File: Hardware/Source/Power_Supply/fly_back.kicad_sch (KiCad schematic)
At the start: 45 parts, among them J1 HB9500M-9.5-3P, U1 TOP270VG, U3 PC817X2NIPW, U4 TL431CLPM

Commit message: update
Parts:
- R11: value 4.99K 1206 1% -> 4.99K/1206/1%
- U2: footprint (none) -> charge_battery_footprint_lib:Transformer_ER35
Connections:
- net at C11.1, U3.4 (C): now also D3.2; no longer D3.
- net at U2.6 (OUT2A): now also D3.1; no longer D3.
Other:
- moved on the sheet: D3
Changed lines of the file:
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@@
 	(wire
 		(pts
-			(xy 257.81 102.87) (xy 264.16 102.87)
+			(xy 254 102.87) (xy 264.16 102.87)
 		)
 		(stroke
@@
 	(wire
 		(pts
-			(xy 238.76 102.87) (xy 247.65 102.87)
+			(xy 238.76 102.87) (xy 243.84 102.87)
 		)
 		(stroke
@@
 			)
 		)
-		(property "Value" "4.99K 1206 1%"
+		(property "Value" "4.99K/1206/1%"
 			(at 307.34 120.6499 90)
 			(effects
@@
 			)
 		)
-		(property "Footprint" ""
+		(property "Footprint" "charge_battery_footprint_lib:Transformer_ER35"
 			(at 228.6 87.63 0)
 			(effects
@@
 	(symbol
 		(lib_id "charge_battery_sym_lib:1N914")
-		(at 247.65 102.87 0)
+		(at 243.84 102.87 0)
 		(unit 1)
 		(exclude_from_sim no)
@@
 		(dnp no)
 		(property "Reference" "D3"
-			(at 252.984 99.568 0)
+			(at 249.174 99.568 0)
 			(effects
 				(font
@@
 		)
 		(property "Value" "1N914"
-			(at 252.984 106.172 0)
+			(at 249.174 106.172 0)
 			(effects
 				(font
@@
 		)
 		(property "Footprint" "charge_battery_footprint_lib:DO-204AH"
-			(at 252.984 109.474 0)
+			(at 249.174 109.474 0)
 			(effects
 				(font
@@
 		)
 		(property "Datasheet" "https://www.mouser.vn/datasheet/2/268/1N914-3499939.pdf"
-			(at 253.492 109.728 0)
+			(at 249.682 109.728 0)
 			(effects
 				(font
@@
 		)
 		(property "Description" "Small Signal Switching Diodes 100 V Signal or Computer Diode"
-			(at 257.81 109.728 0)
+			(at 254 109.728 0)
 			(effects
 				(font
@@
 		)
 		(property "Supply Name" "Mouser"
-			(at 252.73 109.982 0)
+			(at 248.92 109.982 0)
 			(effects
 				(font
@@
 		)
 		(property "Supply Number" "1N914"
-			(at 255.27 109.982 0)
+			(at 251.46 109.982 0)
 			(effects
 				(font
@@
 			)
 		)
-		(pin ""
+		(pin "1"
 		)
-		(pin ""
+		(pin "2"
 		)
 		(instances

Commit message: update
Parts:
- removed U2: ~, charge_battery_footprint_lib:Transformer_ER35, symbol charge_battery_sym_lib:Transformer_flyback
- added L4: EER35_Transformer_Horizontal, charge_battery_footprint_lib:Transformer_ER35_Horizontal, symbol charge_battery_sym_lib:EER35_Transformer_Horizontal
- R1, R2: value 10.2M/1% -> 10.2M/1%/1.25W
- R10: value 6.8R/0805/5% -> 6.8R/5%/1_8W
- R11: value 4.99K/1206/1% -> 4.99K/1%/1_4W
- R13: value 47.5K/1% -> 47.5K/1%/1_8W
- R14: value 12.4K/1% -> 12.4K/1%/1_8W
- R4, R5: value 2M/1% -> 2M/1%/1_10W
- R8: value 5.6R/5% -> 5.6R/5%/1_4W
- R9: value 22R/1206/1% -> 22R/1%/1_4W
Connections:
- net GND2: now also R14.1, U4.3 (A), L4.11 (SC)
- net at C5.1, C6.2, C7.1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: now also L4.1 (AA)
- net at CR2.2, R9.1: now also L4.9 (SA)
- net at CR1.2 (A), U1.6 (D): now also L4.8 (AB)
- net at C11.2: now also L4.16 (SB)
- net at D3.1: now also L4.12 (SC)
- no-connect marks 1 -> 0
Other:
- moved on the sheet: C11, C12, C13, C14, C15, C16, C5, C7, CR2, D1, L2, R4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

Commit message: update pcb flyback
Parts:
- R9: value 22R/1%/1_4W -> 22R/1%/2W; footprint charge_battery_footprint_lib:Res_1206 -> charge_battery_footprint_lib:Res_Hole_2W
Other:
- moved on the sheet: R9
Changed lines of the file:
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@@
 	(wire
 		(pts
-			(xy 254 80.01) (xy 255.27 80.01)
+			(xy 252.73 80.01) (xy 255.27 80.01)
 		)
 		(stroke
@@
 	(wire
 		(pts
-			(xy 242.57 80.01) (xy 246.38 80.01)
+			(xy 242.57 80.01) (xy 245.11 80.01)
 		)
 		(stroke
@@
 	(symbol
 		(lib_id "charge_battery_sym_lib:Res_22R_1206_1%")
-		(at 250.19 76.2 0)
+		(at 248.92 76.2 0)
 		(unit 1)
 		(exclude_from_sim no)
@@
 		(dnp no)
 		(property "Reference" "R9"
-			(at 249.936 75.946 0)
-			(effects
-				(font
-					(size 1.27 1.27)
-				)
-			)
-		)
-		(property "Value" "22R/1%/1_4W"
-			(at 248.412 77.978 0)
-			(effects
-				(font
-					(size 1.27 1.27)
-				)
-			)
-		)
-		(property "Footprint" "charge_battery_footprint_lib:Res_1206"
-			(at 250.19 76.2 0)
+			(at 248.666 75.946 0)
+			(effects
+				(font
+					(size 1.27 1.27)
+				)
+			)
+		)
+		(property "Value" "22R/1%/2W"
+			(at 247.142 77.978 0)
+			(effects
+				(font
+					(size 1.27 1.27)
+				)
+			)
+		)
+		(property "Footprint" "charge_battery_footprint_lib:Res_Hole_2W"
+			(at 248.92 76.2 0)
 			(effects
 				(font
@@
 		)
 		(property "Datasheet" ""
-			(at 250.19 76.2 0)
+			(at 248.92 76.2 0)
 			(effects
 				(font
@@
 		)
 		(property "Description" "Resistor"
-			(at 250.19 76.2 0)
+			(at 248.92 76.2 0)
 			(effects
 				(font
@@
 		)
 		(property "Supply Name" "thegioiic"
-			(at 250.19 76.2 0)
+			(at 248.92 76.2 0)
 			(effects
 				(font
@@
 		)
 		(property "Supply Part Number" "Điện Trở 22 Ohm 1206 1%"
-			(at 250.19 76.2 0)
+			(at 248.92 76.2 0)
 			(effects
 				(font
@@
 		)
 		(property "Supply URL" "https://www.thegioiic.com/dien-tro-22-ohm-1206-1-"
-			(at 250.19 76.2 0)
-			(effects
-				(font
+			(at 248.92 76.2 0)
+			(effects
+				(font

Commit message: tuan uupdate lib
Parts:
- removed L4: EER35_Transformer_Horizontal, charge_battery_footprint_lib:Transformer_ER35_Horizontal, symbol charge_battery_sym_lib:EER35_Transformer_Horizontal
- added T1: Transformer_flyback, charge_battery_footprint_lib:Transformer_ER35_Horizontal, symbol charge_battery_sym_lib:Transformer_flyback
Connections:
- net GND1: now also C11.2, R3.1, T1.5 (OUT2B)
- net GND2: now also T1.11 (OUT1B)
- net at C5.1, C6.2, C7.1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: now also R7.1, T1.1 (IN+)
- net at C6.1, D2.1 (K), R7.2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: now also R6.2
- net at CR2.2, R9.1: now also T1.9 (OUT1A)
- net at CR1.2 (A), U1.6 (D): now also T1.3 (IN-)
- net at D3.1: now also T1.14 (OUT2A)
- net at U1.2 (X): now also R2.1, R3.2; no longer R3.1
- no-connect marks 0 -> 1
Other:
- moved on the sheet: C11, C12, C13, C14, C16, CR2, L2, R6, R7

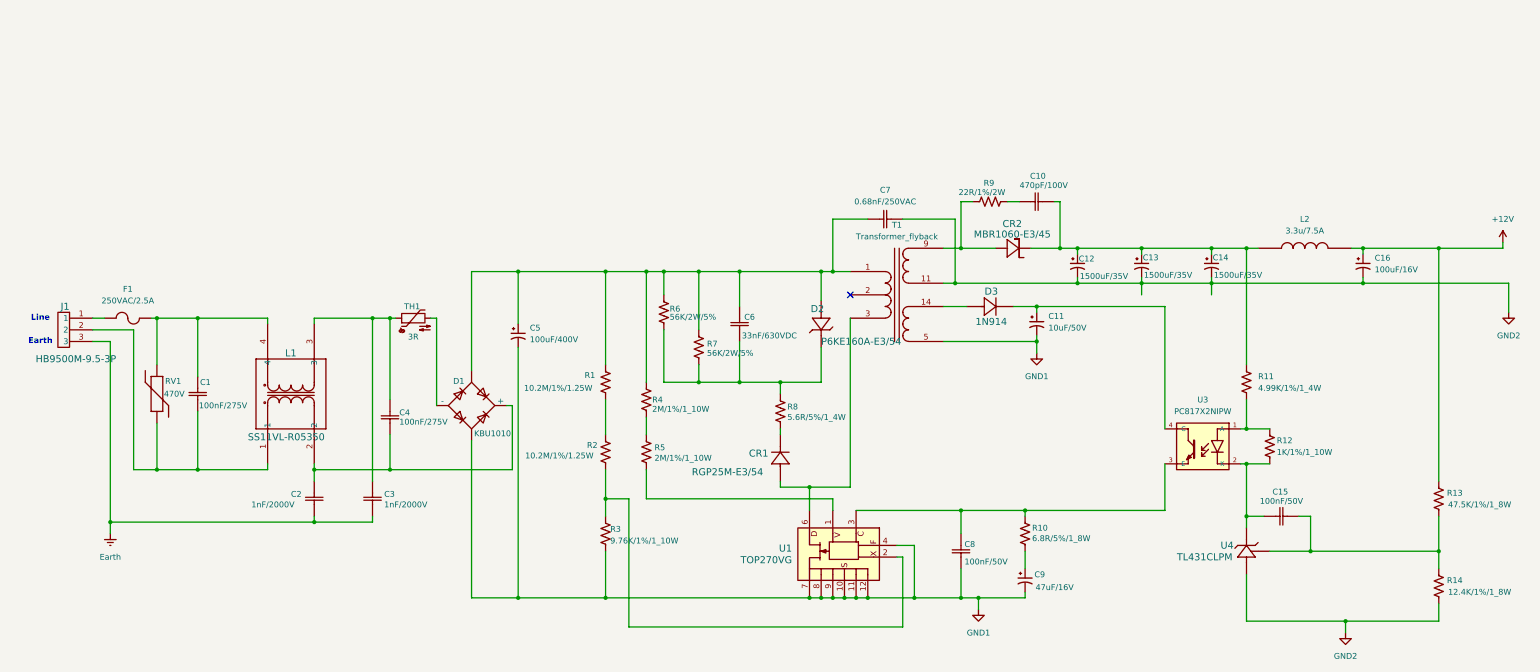
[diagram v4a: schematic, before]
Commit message: flyback 7V
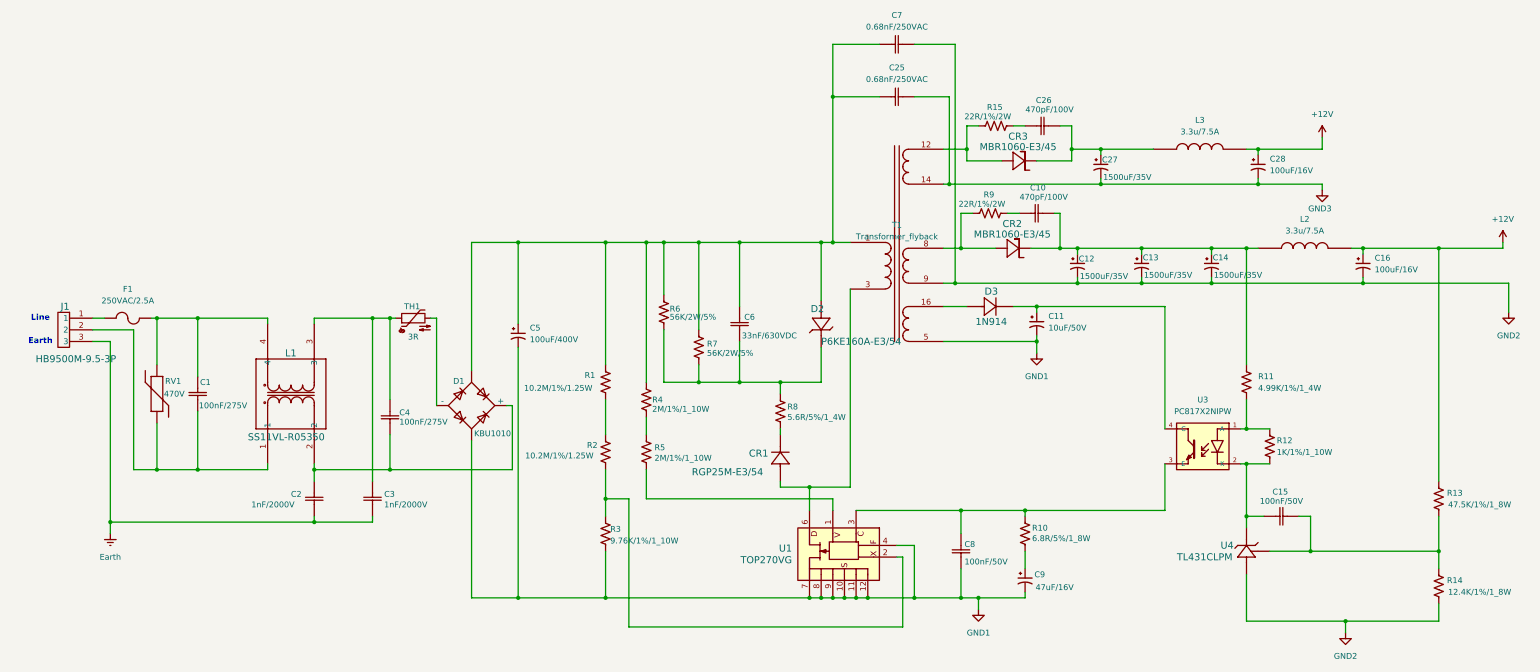
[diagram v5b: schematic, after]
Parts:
- added C25: 0.68nF/250VAC, charge_battery_footprint_lib:Ceramic_Cap_Hole_5mm, symbol charge_battery_sym_lib:EMI_Cap_Hole_0.68nF_250VAC
- added C26: 470pF/100V, charge_battery_footprint_lib:Ceramic_Cap_Hole_5mm, symbol charge_battery_sym_lib:Cap_Hole_470pF_100V
- added C27: 1500uF/35V, Capacitor_THT:CP_Radial_D13.0mm_P5.00mm, symbol charge_battery_sym_lib:Cap_Hole_1500uF_35V
- added C28: 100uF/16V, Capacitor_SMD:CP_Elec_6.3x5.4, symbol charge_battery_sym_lib:Cap_Polarize_100uF_16V
- added CR3: MBR1060-E3/45, charge_battery_footprint_lib:TO-220-2_MCH, symbol charge_battery_sym_lib:MBR1060-E3_45
- added L3: 3.3u/7.5A, charge_battery_footprint_lib:Inductor_3.3u_7447471033, symbol charge_battery_sym_lib:Inductor_3.3u_7.5A
- added R15: 22R/1%/2W, charge_battery_footprint_lib:Res_Hole_2W, symbol charge_battery_sym_lib:Res_22R_1206_1%
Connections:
- net +12V: now also C28.1, L3.2
- net GND2: now also T1.9 (OUT1B); no longer T1.11 (OUT1B)
- net at C5.1, C6.2, C7.1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: now also C25.1
- net at CR2.2, R9.1: now also T1.8 (OUT1A); no longer T1.9 (OUT1A)
- net at D3.1: now also T1.16 (OUT2A); no longer T1.14 (OUT2A)
- new net: C26.2, C27.1, CR3.1, L3.1
- new net: CR3.2, R15.1, T1.12 (OUT1A)
- new net: C26.1, R15.2
- new net GND3: C25.2, C27.2, C28.2, T1.14 (OUT1B)
- no-connect marks 1 -> 0
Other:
- moved on the sheet: C10, C7, R9

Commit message: update
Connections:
- net +12V: no longer C28.1, L3.2
- new net +7V: C28.1, L3.2
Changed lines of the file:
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@@
 			)
 		)
-		(property "Value" "+12V"
+		(property "Value" "+7V"
 			(at 321.31 60.96 0)
 			(effects

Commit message: update sche
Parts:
- removed L1: SS11VL-R05350, charge_battery_footprint_lib:IND_SS11VL-R05350_KEM, symbol charge_battery_sym_lib:SS11VL-R05350
- added FL1: SC-02-E60JKH, charge_battery_footprint_lib:SC02E60JKH, symbol charge_battery_sym_lib:SC-02-E60JKH
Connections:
- net at C2.1, C4.1, D1.1 (+): now also FL1.2
- net at C1.1, J1.2, RV1.1: now also FL1.1
- net at C1.2, F1.2, RV1.2: now also FL1.4
- net at C3.1, C4.2, TH1.1: now also FL1.3
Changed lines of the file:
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@@
-	)
-	(symbol
-		(lib_id "charge_battery_sym_lib:SS11VL-R05350")
-		(at 91.44 137.16 90)
-		(unit 1)
-		(exclude_from_sim no)
-		(in_bom yes)
-		(on_board yes)
-		(dnp no)
-		(property "Reference" "L1"
-			(at 95.25 113.03 90)
-			(effects
-				(font
-					(size 1.524 1.524)
-				)
-				(justify right)
-			)
-		)
-		(property "Value" "SS11VL-R05350"
-			(at 87.122 131.318 90)
-			(effects
-				(font
-					(size 1.524 1.524)
-				)
-				(justify right)
-			)
-		)
-		(property "Footprint" "charge_battery_footprint_lib:IND_SS11VL-R05350_KEM"
-			(at 111.506 137.922 0)
-			(effects
-				(font
-					(size 1.27 1.27)
-					(italic yes)
-				)
-				(hide yes)
-			)
-		)
-		(property "Datasheet" "https://www.mouser.vn/datasheet/2/447/KEM_LF0022_SS11VL-3316893.pdf"
-			(at 111.252 132.588 0)
-			(effects
-				(font
-					(size 1.27 1.27)
-					(italic yes)
-				)
-				(hide yes)
-			)
-		)
-		(property "Description" "Common Mode Chokes / Filters 250VAC 1.1A 5mH DCR=400mOhms"
-			(at 111.506 135.382 0)
-			(effects
-				(font
-					(size 1.27 1.27)
-				)
-				(hide yes)
-			)
-		)
-		(property "Supply name" "Mouser"
-			(at 111.506 137.668 0)
-			(effects
-				(font
-					(size 1.27 1.27)
-				)
-				(hide yes)
-			)
-		)
-		(property "Supply part number" "80-SS11VL-11050"
-			(at 111.506 137.16 0)
-			(effects
-				(font
-					(size 1.27 1.27)
-				)
-				(hide yes)
-			)
-		)
-		(property "Supply URL" "https://www.mouser.vn/ProductDetail/KEMET/SS11VL-11050?qs=EU6FO9ffTwcryP%252B%2F%252BYgxUg%3D%3D"
-			(at 111.506 149.352 0)
-			(effects
-				(font
-					(size 1.27 1.27)
-				)
-				(hide yes)
-			)
-		)
-		(pin "1"
-		)
-		(pin "2"
-		)
-		(pin "3"
-		)
-		(pin "4"
-		)
-		(instances
-			(project "Power_Supply"
-				(path "/5c8a7907-026b-4416-b231-5ef9f93b99e1/5a1d07e8-1900-453e-ab71-30ad5bc9dcd9"
-					(reference "L1")
-					(unit 1)
-				)
-			)
-		)
 	)
 	(symbol
@@
 					(unit 1)
 				)
+			)
+		)
+	)
+	(symbol
+		(lib_id "charge_battery_sym_lib:SC-02-E60JKH")
+		(at 85.09 121.92 90)
+		(unit 1)
+		(exclude_from_sim no)
+		(in_bom yes)
+		(on_board yes)
+		(dnp no)
+		(fields_autoplaced yes)
+		(property "Reference" "FL1"
+			(at 105.41 121.9199 90)
+			(effects
+				(font
+					(size 1.27 1.27)
+				)
+				(justify right)
+			)
+		)
+		(property "Value" "SC-02-E60JKH"
+			(at 108.204 130.556 0)
+			(effects
+				(font
+					(size 1.27 1.27)
+				)
+				(justify left top)
+				(hide yes)
+			)
+		)
+		(property "Footprint" "charge_battery_footprint_lib:SC02E60JKH"
+			(at 180.01 105.41 0)
+			(effects
+				(font
+					(size 1.27 1.27)
+				)
+				(justify left top)
+				(hide yes)
+			)
+		)
+		(property "Datasheet" "https://content.kemet.com/datasheets/KEM_LF0076_SC-JKH.pdf"
+			(at 280.01 105.41 0)
+			(effects
+				(font
+					(size 1.27 1.27)
+				)
+				(justify left top)
+				(hide yes)
+			)
+		)
+		(property "Description" "KEMET, SC_JKH, AC Line Filters, Common Mode, 250 VAC, 6 mH, 2 A, 120C, -25C, 100 mOhms, 320, 24.5mm, 24.5mm, 17mm, 3.5mm, 11mm, 18mm, 13 g"
+			(at 108.966 123.19 0)
+			(effects
+				(font
+					(size 1.27 1.27)
+				)
+				(hide yes)
+			)
+		)
+		(property "Height" "17"
+			(at 480.01 105.41 0)
+			(effects
+				(font
+					(size 1.27 1.27)
+				)
+				(justify left top)
+				(hide yes)
+			)
+		)
+		(property "Mouser Part Number" "80-SC-02-E60JKH"
+			(at 580.01 105.41 0)
+			(effects
+				(font
+					(size 1.27 1.27)
+				)
+				(justify left top)
+				(hide yes)
+			)
+		)
+		(property "Mouser Price/Stock" "https://www.mouser.co.uk/ProductDetail/KEMET/SC-02-E60JKH?qs=PzGy0jfpSMtza3nlRmZjgA%3D%3D"
+			(at 680.01 105.41 0)
+			(effects
+				(font
+					(size 1.27 1.27)
+				)
+				(justify left top)
+				(hide yes)
+			)
+		)
+		(property "Manufacturer_Name" "KEMET"
+			(at 780.01 105.41 0)
+			(effects
+				(font
+					(size 1.27 1.27)
+				)
+				(justify left top)
+				(hide yes)
+			)
+		)
+		(property "Manufacturer_Part_Number" "SC-02-E60JKH"
+			(at 880.01 105.41 0)
+			(effects
+				(font
+					(size 1.27 1.27)
+				)
+				(justify left top)
+				(hide yes)
+			)
+		)
+		(pin "1"
+		)
+		(pin "2"
+		)
+		(pin "4"
+		)
+		(pin "3"
+		)
+		(instances
+			(project ""
+				(path "/5c8a7907-026b-4416-b231-5ef9f93b99e1/5a1d07e8-1900-453e-ab71-30ad5bc9dcd9"
+					(reference "FL1")
+					(unit 1)
+				)

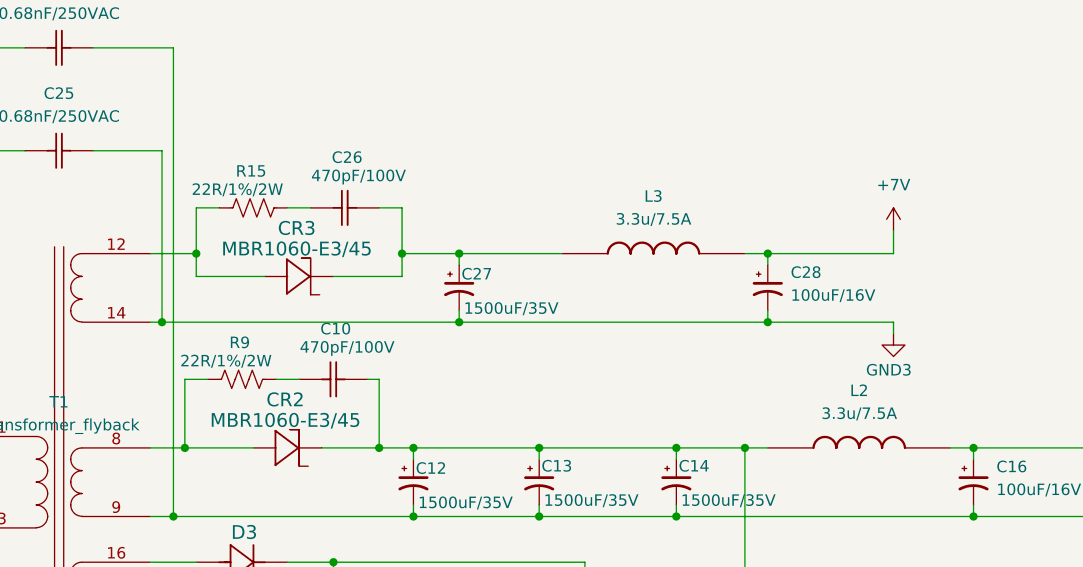
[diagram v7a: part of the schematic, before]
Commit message: update flyback co 7V
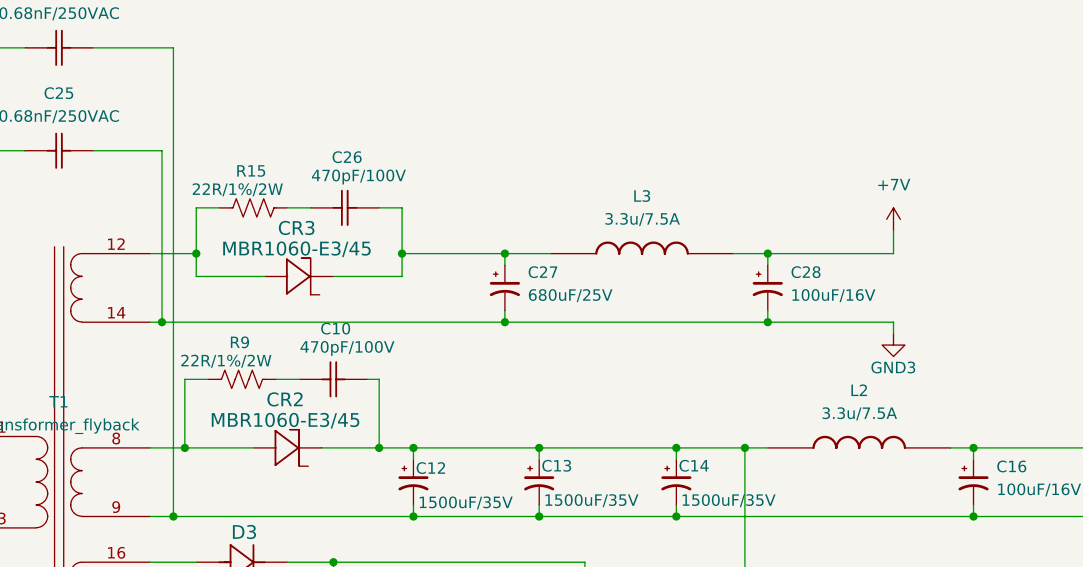
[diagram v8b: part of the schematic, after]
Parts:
- removed C27: 1500uF/35V, Capacitor_THT:CP_Radial_D13.0mm_P5.00mm, symbol charge_battery_sym_lib:Cap_Hole_1500uF_35V
- added C27: 680uF/25V, Capacitor_SMD:CP_Elec_10x10.5, symbol charge_battery_sym_lib:Cap_Polarized_SMD_680uF_25V
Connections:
- net GND3: now also C27.2
- net at C26.2, CR3.1, L3.1: now also C27.1
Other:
- moved on the sheet: L3
